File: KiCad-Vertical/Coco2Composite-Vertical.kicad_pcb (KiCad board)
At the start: 2 copper layers, 65.1 x 39.7 mm, 17 parts, among them J1 TO_COCO2, J2 AUDIO_JACK_3.5MM_KIT, Q1 PN2907, Q2 2N2222, U1 MC1372

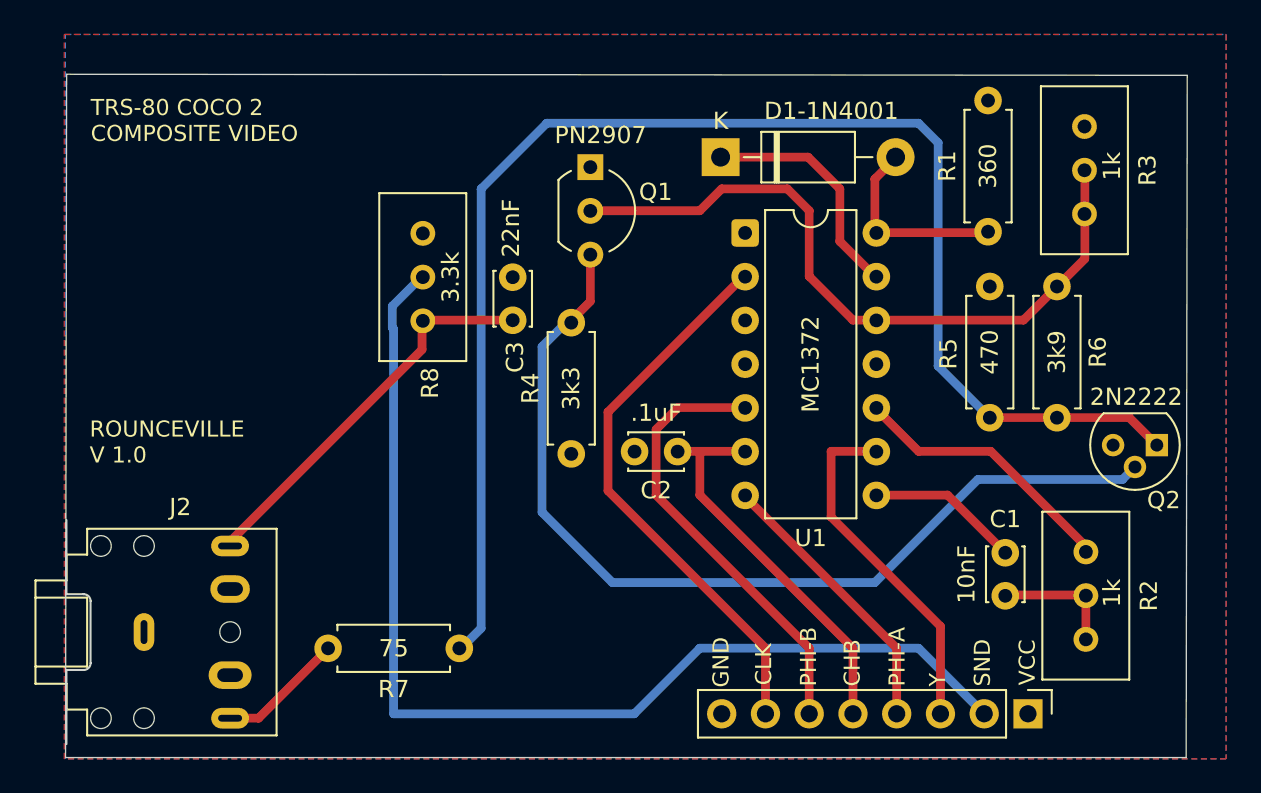
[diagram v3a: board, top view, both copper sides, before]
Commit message: Overhauled vertical board based on lessons learned working on horizontal board
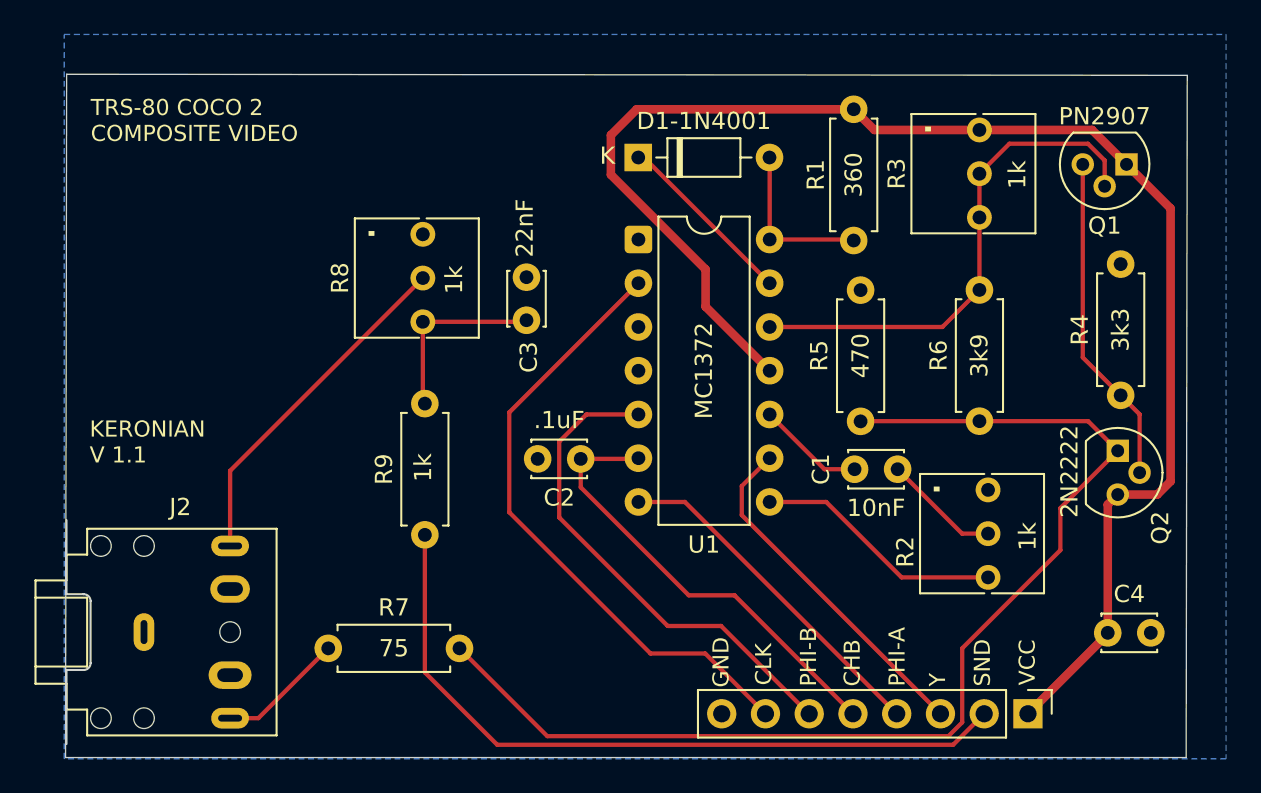
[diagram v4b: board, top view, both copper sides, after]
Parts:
- added C4: 1uF, Capacitor_THT:C_Disc_D3.0mm_W2.0mm_P2.50mm, F.Cu at (176.4, 117.6)
- added R9: 1k, Resistor_THT:R_Axial_DIN0207_L6.3mm_D2.5mm_P7.62mm_Horizontal, F.Cu at (136.8, 111.9)
- D1-1N4001: value 1N4004 -> 1N4148; footprint Diode_THT:D_DO-41_SOD81_P10.16mm_Horizontal -> Diode_THT:D_DO-35_SOD27_P7.62mm_Horizontal
- Q1: footprint Package_TO_SOT_THT:TO-92_Inline_Wide -> Package_TO_SOT_THT:TO-92
- R2, R3: footprint Potentiometer_THT:Potentiometer_Bourns_3296W_Vertical -> Modified:Potentiometer_Bourns_3266Y_Vertical
- R8: value 3.3k -> 1k; footprint Potentiometer_THT:Potentiometer_Bourns_3296W_Vertical -> Modified:Potentiometer_Bourns_3266Y_Vertical
- moved R4 32.1 mm to (177.2, 103.8)
- moved Q1 31.1 mm to (177.5, 90.4), turned to 180 degrees
- moved R5 10.8 mm to (162.1, 105.3), turned to 90 degrees
- moved R1 10.6 mm to (161.7, 87.2), turned to -90 degrees
- moved R2 10.4 mm to (169.5, 109.3), turned to 90 degrees
- moved C1 10.0 mm to (161.8, 108.1), turned to 0 degrees
- moved R6 9.02 mm to (169.0, 105.3), turned to 90 degrees
- moved R3 7.81 mm to (169.0, 88.4), turned to 90 degrees
- moved R7 7.61 mm to (131.2, 118.5), turned to 0 degrees
- moved U1 6.21 mm to (149.2, 94.8)
- moved C2 5.64 mm to (145.8, 107.5)
- moved R8 5.02 mm to (136.7, 94.5), turned to 90 degrees
- moved D1-1N4001 4.78 mm to (149.2, 90.0)
- moved Q2 2.29 mm to (177.0, 107.0), turned to -90 degrees
- moved C3 0.80 mm to (142.7, 99.5)
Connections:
- net Net-(U1-COL_A_IN) renamed /PHI-A
- net Net-(U1-COL_B_IN) renamed /PHI-B
- net Net-(U1-COL_REF_IN) renamed /CHB
- net Net-(U1-LUM_IN) renamed /Y
- net Net-(U1-OSC_IN) renamed /CLK
- C1 pad 1: Net-(U1-CHROM_MOD_OUT) -> Net-(U1-CHROM_IN)
- D1-1N4001 pad 2: Net-(U1-RF_TANK_2) -> Net-(D1-1N4001-A)
- J1 pad 2: Net-(J1-Pad2) -> /SND
- J2 pad R: Net-(C3-Pad1) -> /SND_OUT
- J2 pad S: GND -> (no net)
- J2 pad T: Net-(J2-PadTIP) -> /COMP_OUT
- R1 pad 1: Net-(U1-RF_TANK_2) -> VCC
- R1 pad 2: VCC -> Net-(D1-1N4001-A)
- R2 pad 1: Net-(C1-Pad2) -> GND
- R2 pad 3: Net-(U1-CHROM_IN) -> Net-(U1-CHROM_MOD_OUT)
- R3 pad 1: Net-(U1-RF_OUT) -> VCC
- R3 pad 3: VCC -> Net-(U1-RF_OUT)
- R4 pad 1: GND -> Net-(Q2-B)
- R4 pad 2: Net-(Q2-B) -> GND
- R5 pad 1: GND -> Net-(Q2-E)
- R5 pad 2: Net-(Q2-E) -> GND
- R6 pad 1: Net-(U1-RF_OUT) -> Net-(Q2-E)
- R6 pad 2: Net-(Q2-E) -> Net-(U1-RF_OUT)
- R7 pad 1: Net-(Q2-E) -> /COMP_OUT
- R7 pad 2: Net-(J2-PadTIP) -> Net-(Q2-E)
- R8 pad 1: Net-(C3-Pad1) -> GND
- R8 pad 2: Net-(J1-Pad2) -> /SND_OUT
- R8 pad 3: (no net) -> Net-(C3-Pad1)
- U1 pad 14: Net-(U1-RF_TANK_2) -> Net-(D1-1N4001-A)
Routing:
- net VCC: track 0.00 -> 87.2 mm
- net Net-(J1-Pad2): track 63.6 -> 0.00 mm
- net /SND: track 0.00 -> 43.0 mm
- net Net-(Q2-B): track 55.0 -> 19.3 mm
- net /SND_OUT: track 0.00 -> 20.2 mm
- net Net-(Q2-E): track 83.4 -> 66.9 mm
- net Net-(C3-Pad1): track 23.4 -> 10.9 mm
- net Net-(U1-RF_OUT): track 41.2 -> 29.7 mm
- net Net-(U1-RF_TANK_2): track 11.5 -> 0.00 mm
- net Net-(D1-1N4001-A): track 0.00 -> 9.67 mm
- net Net-(U1-CHROM_IN): track 15.9 -> 6.25 mm
- net /COMP_OUT: track 0.00 -> 7.38 mm
- net Net-(J2-PadTIP): track 7.03 -> 0.00 mm
- net Net-(U1-CHROM_MOD_OUT): track 8.96 -> 14.5 mm
- net /PHI-A: track 16.4 -> 20.1 mm
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- removed copper zone on F.Cu, net VCC
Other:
- board text added: "KERONIAN V 1.1"
- board text removed: "ROUNCEVILLE V 1.0"

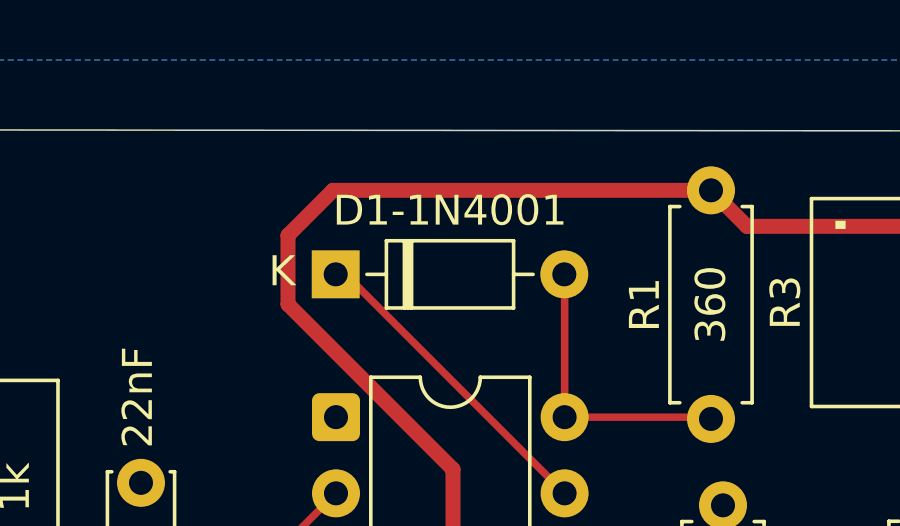
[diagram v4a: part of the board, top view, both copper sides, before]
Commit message: Fixed label on diode
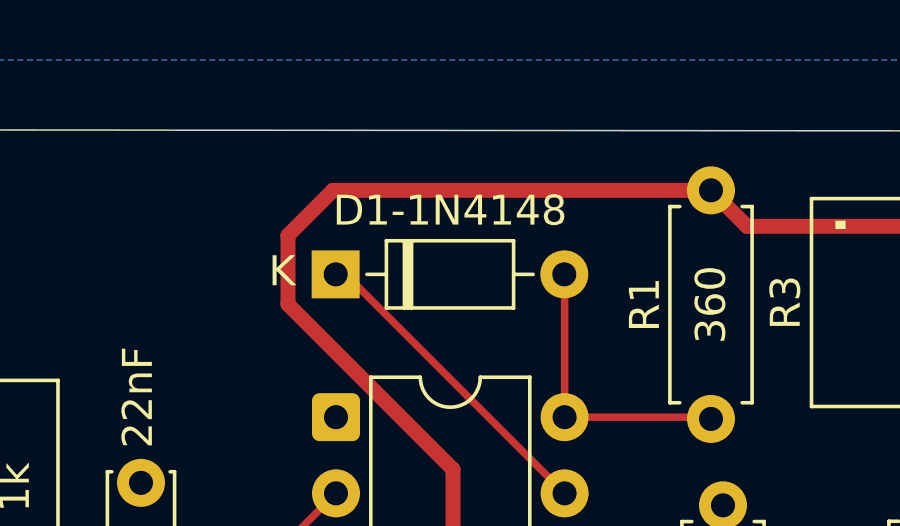
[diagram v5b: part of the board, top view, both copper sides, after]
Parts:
- renumbered D1-1N4001 to D1-1N4148
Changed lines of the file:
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@@
 		(descr "Diode, DO-35_SOD27 series, Axial, Horizontal, pin pitch=7.62mm, , length*diameter=4*2mm^2, , http://www.diodes.com/_files/packages/DO-35.pdf")
 		(tags "Diode DO-35_SOD27 series Axial Horizontal pin pitch 7.62mm  length 4mm diameter 2mm")
-		(property "Reference" "D1-1N4001"
+		(property "Reference" "D1-1N4148"
 			(at 3.81 -2.12 0)
 			(layer "F.SilkS")

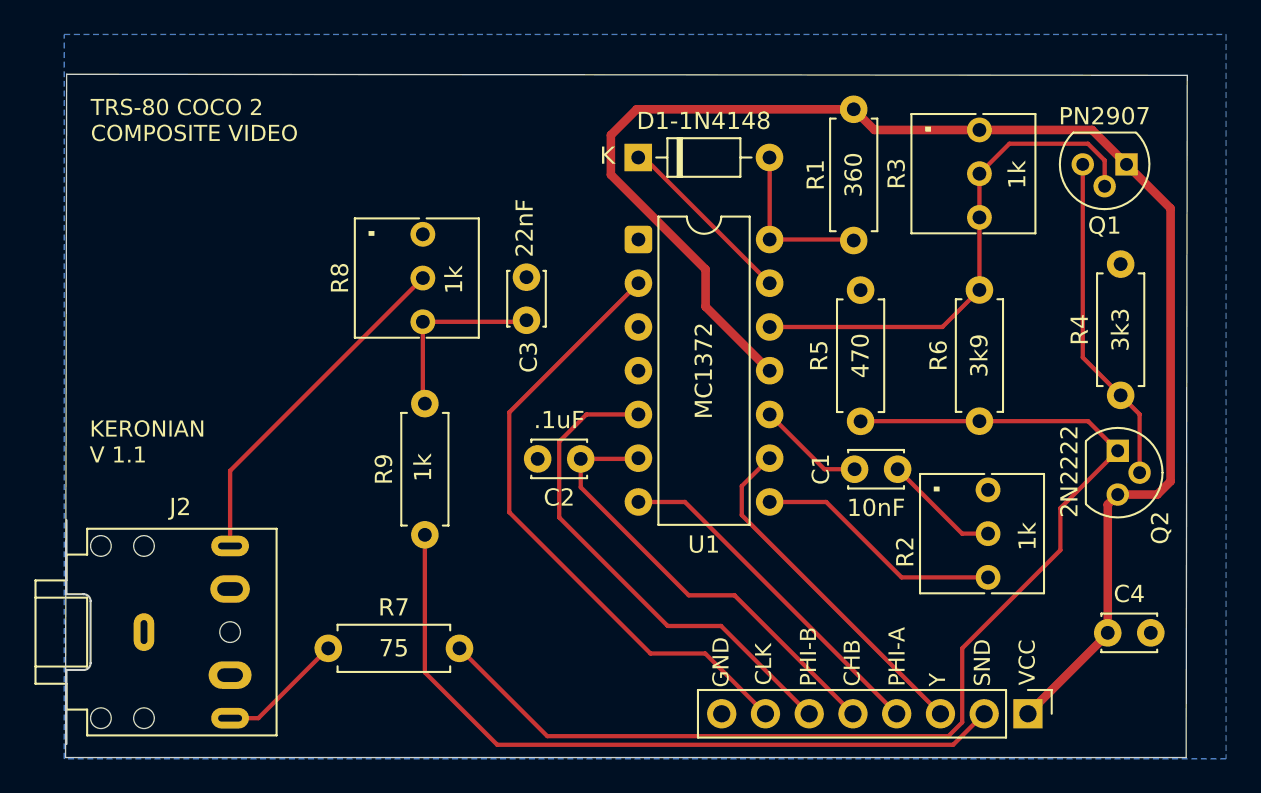
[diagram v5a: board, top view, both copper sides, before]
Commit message: Updated some schematic symbols and rerouted a few things on the vertical board
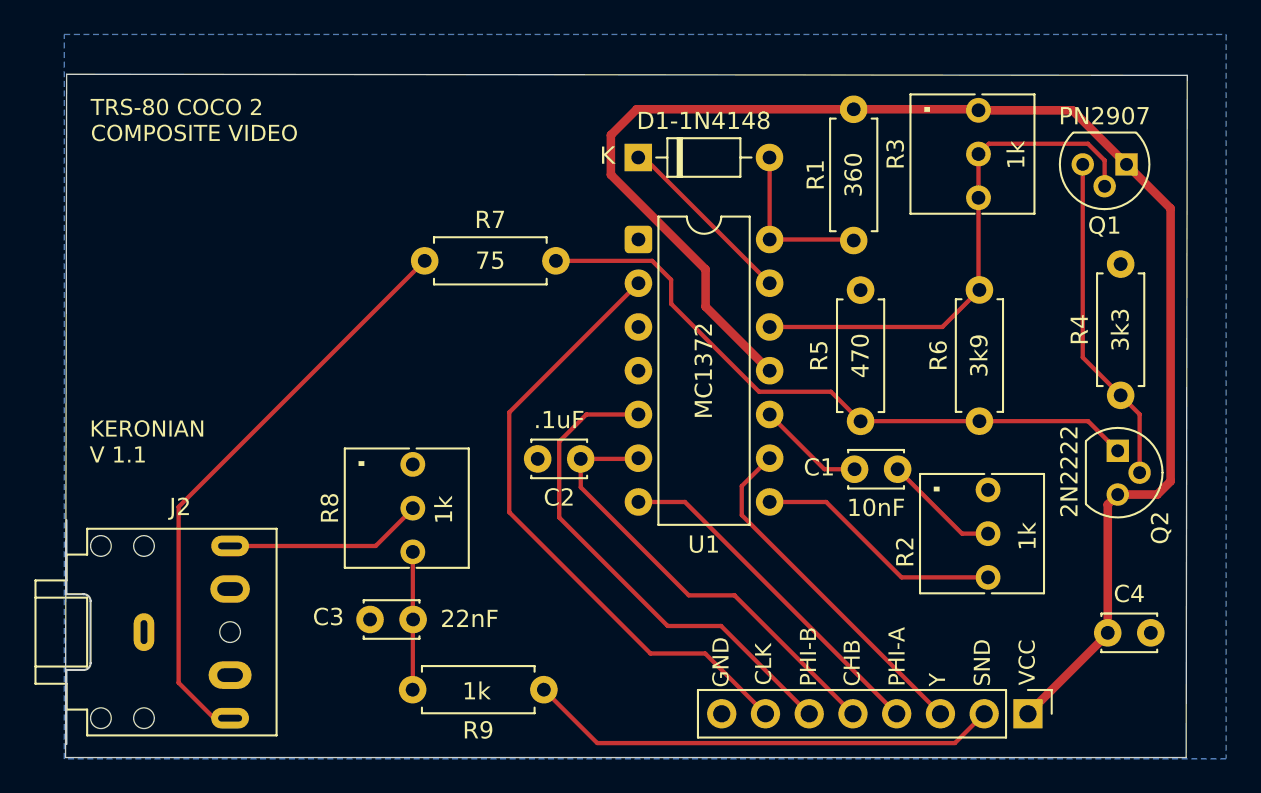
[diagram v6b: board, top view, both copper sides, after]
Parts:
- moved R7 23.2 mm to (136.8, 96.0)
- moved C3 18.6 mm to (136.1, 116.8), turned to 180 degrees
- moved R8 13.4 mm to (136.1, 107.8)
- moved R9 11.3 mm to (143.7, 120.9), turned to 180 degrees
- moved R3 1.14 mm to (168.9, 87.3)
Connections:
- J2 pad S: (no net) -> GND
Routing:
- net Net-(Q2-E): track 66.9 -> 38.1 mm
- net /COMP_OUT: track 7.38 -> 34.3 mm
- net /SND: track 43.0 -> 27.6 mm
- net /SND_OUT: track 20.2 -> 11.5 mm
- net Net-(C3-Pad1): track 10.9 -> 8.01 mm
- net Net-(U1-RF_OUT): track 29.7 -> 30.5 mm

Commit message: Added color switch to vertical board
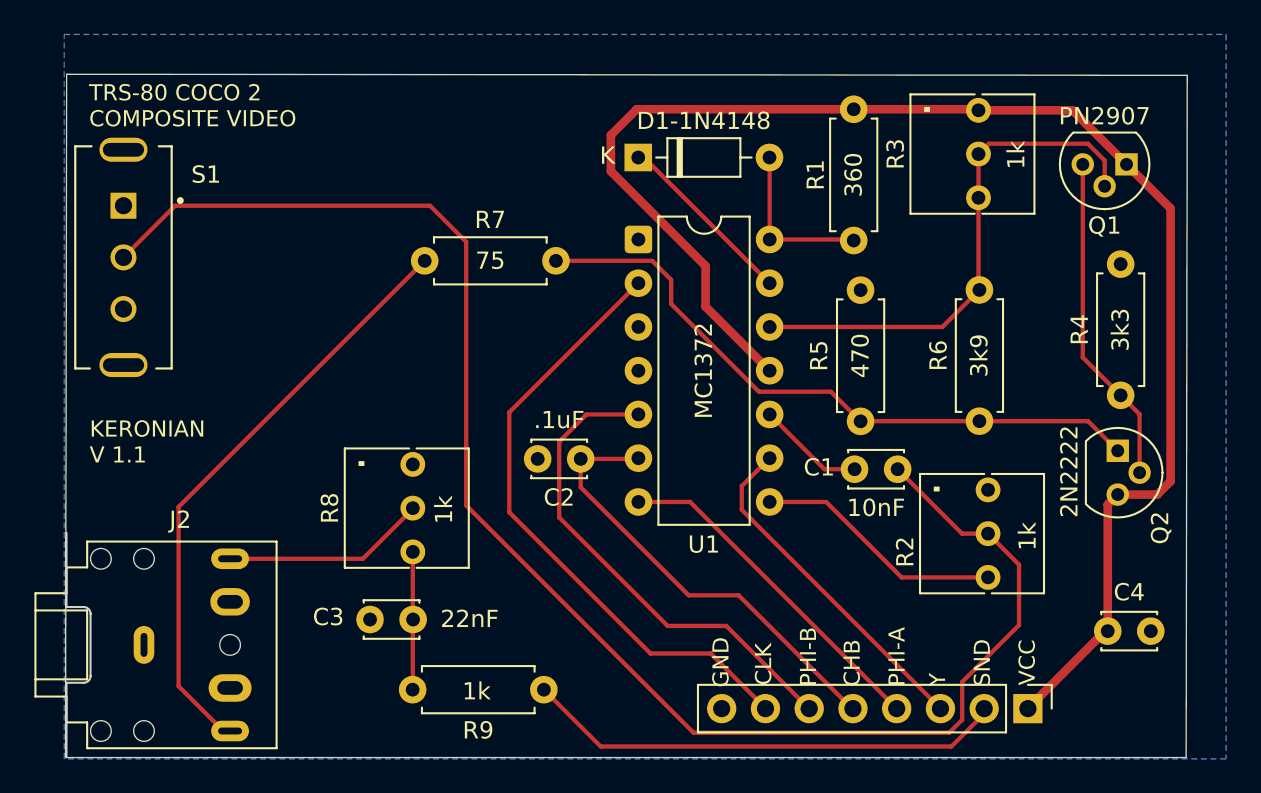
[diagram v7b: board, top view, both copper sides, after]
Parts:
- added S1: SW_SLW-1298856-5A-RA-N-D, Imported:SW_SLW-1298856-5A-RA-N-D, F.Cu at (119.3, 95.8)
- moved J2 0.74 mm to (120.5, 118.3)
- moved J1 0.30 mm to (171.8, 122.0)
- moved C4 0.10 mm to (176.4, 117.5)
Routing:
- net Net-(C1-Pad2): track 6.80 -> 91.6 mm
